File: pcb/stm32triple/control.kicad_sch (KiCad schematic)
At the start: 25 parts, among them J1 USB_C_Receptacle_USB2.0, P1 ST-Link, P2 ST-Link, P3 UG-2864ASWPG01, SW1 RotaryEncoder_Switch, U1 STM32G431CBUx, U3 BME680, U7 TPS82130

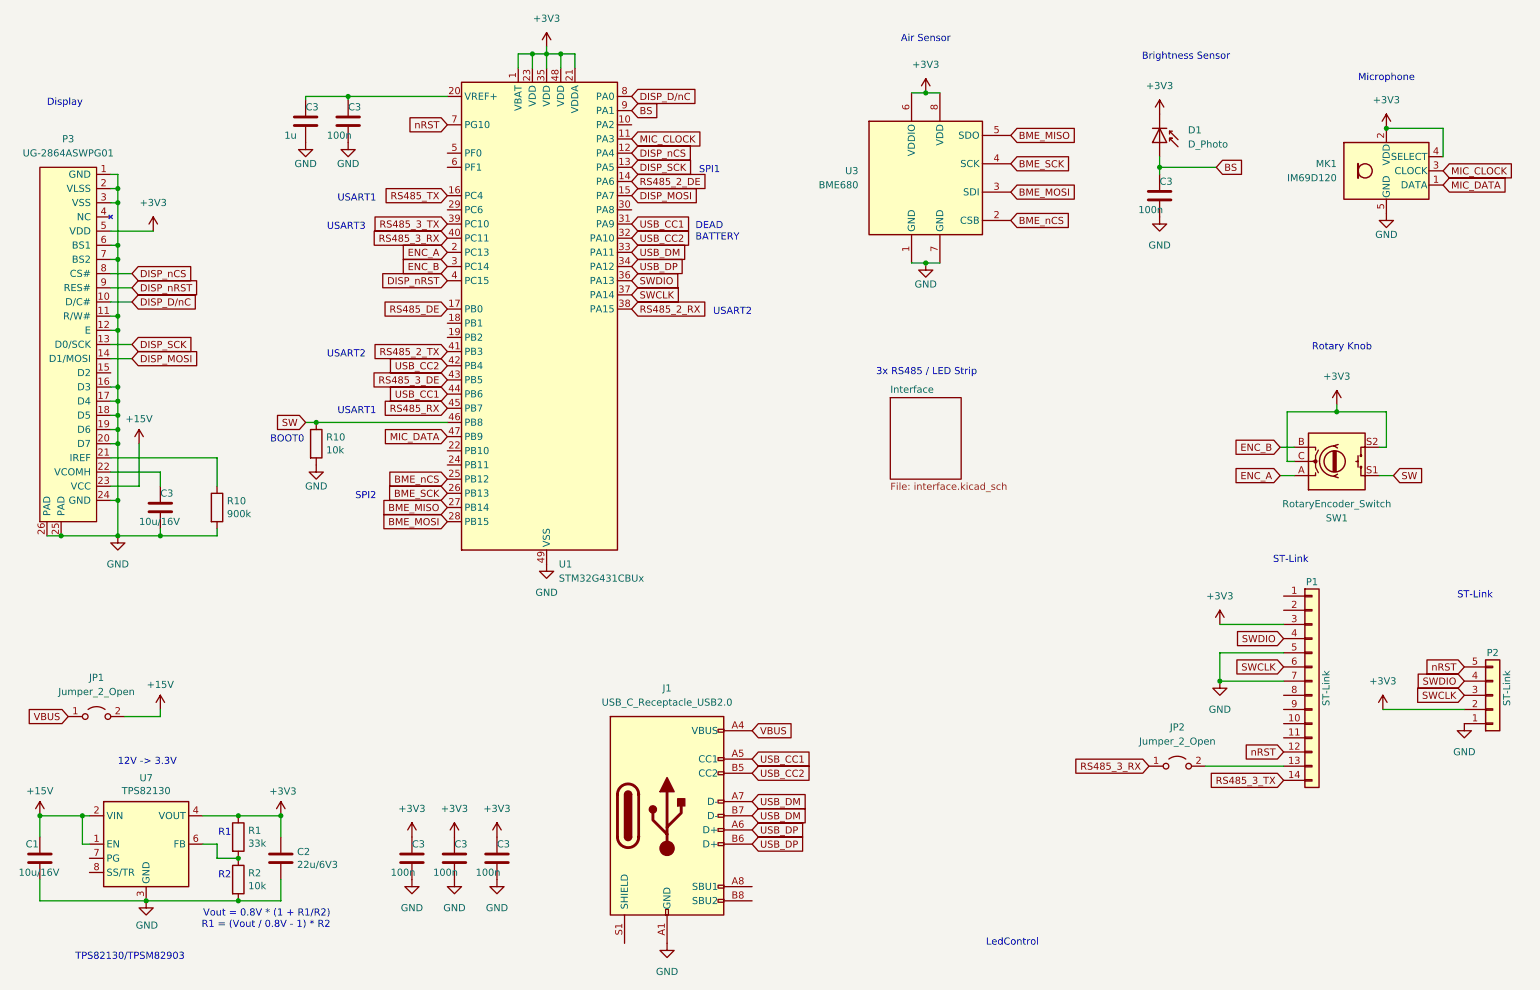
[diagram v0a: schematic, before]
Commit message: Add IR receiver
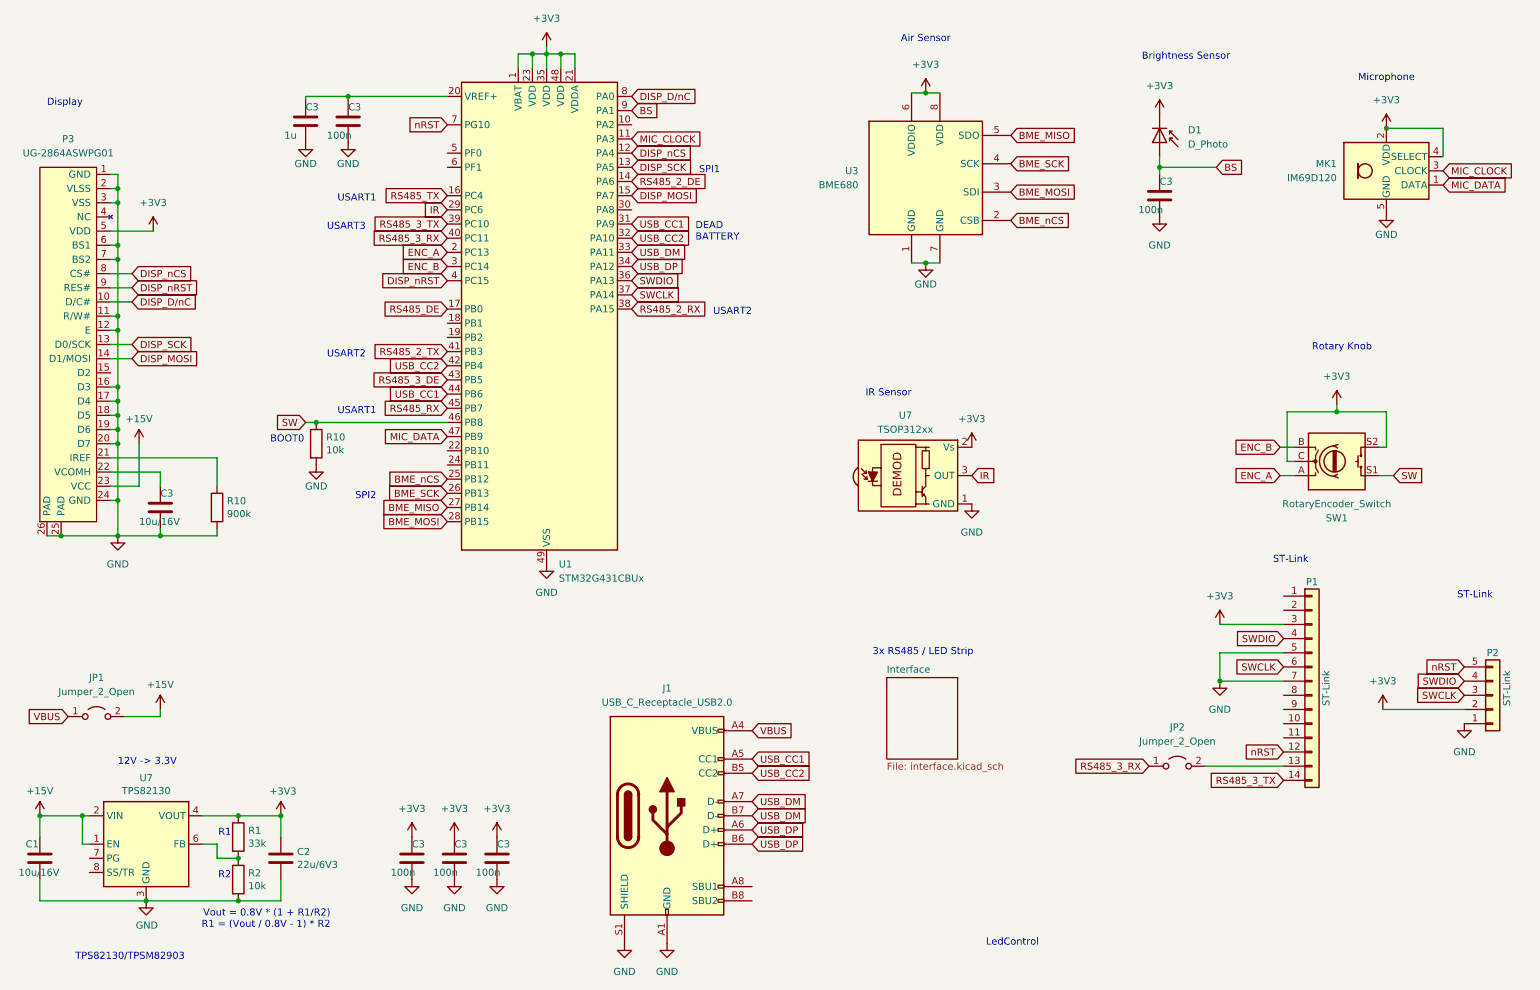
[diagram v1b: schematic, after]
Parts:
- added U7: TSOP312xx, local:TSOP31238, symbol Interface_Optical:TSOP312xx
- J1: footprint local:USB4510-03-1-A -> local:USB4105-GF-A-120
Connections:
- net +3V3: now also U7.2 (Vs)
- net GND: now also J1.S1 (SHIELD), U7.1 (GND)
- net IR: now reaches U1.29 (PC6)
- net IR: now also U7.3 (OUT)
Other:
- note added: "IR Sensor"
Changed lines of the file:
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@@
     (effects (font (size 1.27 1.27)) (justify left bottom))
   )
-  (text "3x RS485 / LED Strip" (at 168.91 88.265 0)
+  (text "3x RS485 / LED Strip" (at 168.275 138.43 0)
     (effects (font (size 1.27 1.27)) (justify left bottom))
   )
@@
     (effects (font (size 1.27 1.27)) (justify left bottom))
   )
+  (text "IR Sensor" (at 167.005 92.075 0)
+    (effects (font (size 1.27 1.27)) (justify left bottom))
+  )
   (text "SPI1" (at 137.16 52.07 0)
     (effects (font (size 1.27 1.27)) (justify left bottom))
@@
     )
   )
+  (global_label "IR" (shape input) (at 186.055 106.045 0) (fields_autoplaced)
+    (effects (font (size 1.27 1.27)) (justify left))
+    (property "Intersheetrefs" "${INTERSHEET_REFS}" (at 190.915 106.045 0)
+      (effects (font (size 1.27 1.27)) (justify left) hide)
+    )
+  )
   (global_label "RS485_3_DE" (shape input) (at 92.075 88.9 180)
     (effects (font (size 1.27 1.27)) (justify right))
@@
     (property "Intersheetrefs" "${INTERSHEET_REFS}" (at 136.6073 63.5 0)
       (effects (font (size 1.27 1.27)) (justify left) hide)
+    )
+  )
+  (global_label "IR" (shape input) (at 92.075 58.42 180) (fields_autoplaced)
+    (effects (font (size 1.27 1.27)) (justify right))
+    (property "Intersheetrefs" "${INTERSHEET_REFS}" (at 87.215 58.42 0)
+      (effects (font (size 1.27 1.27)) (justify right) hide)
     )
   )
@@
         (path "/4b540715-c4ed-4902-8525-92fb403f6b2e"
           (reference "U3") (unit 1)
+        )
+      )
+    )
+  )
+  (symbol (lib_id "power:GND") (at 123.825 189.865 0) (unit 1)
+    (in_bom yes) (on_board yes) (dnp no) (fields_autoplaced)
+    (property "Reference" "#PWR010" (at 123.825 196.215 0)
+      (effects (font (size 1.27 1.27)) hide)
+    )
+    (property "Value" "GND" (at 123.825 194.945 0)
+      (effects (font (size 1.27 1.27)))
+    )
+    (property "Footprint" "" (at 123.825 189.865 0)
+      (effects (font (size 1.27 1.27)) hide)
+    )
+    (property "Datasheet" "" (at 123.825 189.865 0)
+      (effects (font (size 1.27 1.27)) hide)
+    )
+    (pin "1")
+    (instances
+      (project "Display"
+        (path "/1d03a724-b61f-4021-9dcb-6a5edf10ce9e"
+          (reference "#PWR010") (unit 1)
+        )
+      )
+      (project "control"
+        (path "/4b540715-c4ed-4902-8525-92fb403f6b2e"
+          (reference "#PWR054") (unit 1)
         )
       )
@@
         (path "/4b540715-c4ed-4902-8525-92fb403f6b2e"
           (reference "#PWR024") (unit 1)
+        )
+      )
+    )
+  )
+  (symbol (lib_id "power:GND") (at 186.055 111.125 0) (unit 1)
+    (in_bom yes) (on_board yes) (dnp no) (fields_autoplaced)
+    (property "Reference" "#PWR010" (at 186.055 117.475 0)
+      (effects (font (size 1.27 1.27)) hide)
+    )
+    (property "Value" "GND" (at 186.055 116.205 0)
+      (effects (font (size 1.27 1.27)))
+    )
+    (property "Footprint" "" (at 186.055 111.125 0)
+      (effects (font (size 1.27 1.27)) hide)
+    )
+    (property "Datasheet" "" (at 186.055 111.125 0)
+      (effects (font (size 1.27 1.27)) hide)
+    )
+    (pin "1")
+    (instances
+      (project "Display"
+        (path "/1d03a724-b61f-4021-9dcb-6a5edf10ce9e"
+          (reference "#PWR010") (unit 1)
+        )
+      )
+      (project "control"
+        (path "/4b540715-c4ed-4902-8525-92fb403f6b2e"
+          (reference "#PWR052") (unit 1)
         )
       )
@@
     )
   )
+  (symbol (lib_id "power:+3V3") (at 186.055 100.965 0) (unit 1)
+    (in_bom yes) (on_board yes) (dnp no) (fields_autoplaced)
+    (property "Reference" "#PWR02" (at 186.055 104.775 0)
+      (effects (font (size 1.27 1.27)) hide)
+    )
+    (property "Value" "+3V3" (at 186.055 95.885 0)
+      (effects (font (size 1.27 1.27)))
+    )
+    (property "Footprint" "" (at 186.055 100.965 0)
+      (effects (font (size 1.27 1.27)) hide)
+    )
+    (property "Datasheet" "" (at 186.055 100.965 0)
+      (effects (font (size 1.27 1.27)) hide)
+    )
+    (pin "1")
+    (instances
+      (project "Display"
+        (path "/1d03a724-b61f-4021-9dcb-6a5edf10ce9e"
+          (reference "#PWR02") (unit 1)
+        )
+      )
+      (project "control"
+        (path "/4b540715-c4ed-4902-8525-92fb403f6b2e"
+          (reference "#PWR053") (unit 1)
+        )
+      )
+    )
+  )
   (symbol (lib_id "power:+15V") (at 40.64 147.955 0) (unit 1)
     (in_bom yes) (on_board yes) (dnp no) (fields_autoplaced)
@@
         (path "/4b540715-c4ed-4902-8525-92fb403f6b2e"
           (reference "#PWR018") (unit 1)
+        )
+      )
+    )
+  )
+  (symbol (lib_id "Interface_Optical:TSOP312xx") (at 175.895 106.045 0) (unit 1)
+    (in_bom yes) (on_board yes) (dnp no) (fields_autoplaced)
+    (property "Reference" "U7" (at 174.16 95.25 0)
+      (effects (font (size 1.27 1.27)))
+    )
+    (property "Value" "TSOP312xx" (at 174.16 97.79 0)
+      (effects (font (size 1.27 1.27)))
+    )
+    (property "Footprint" "local:TSOP31238" (at 174.625 115.57 0)
+      (effects (font (size 1.27 1.27)) hide)
+    )
+    (property "Datasheet" "http://www.vishay.com/docs/82492/tsop312.pdf" (at 192.405 98.425 0)
+      (effects (font (size 1.27 1.27)) hide)
+    )
+    (pin "1")
+    (pin "2")
+    (pin "3")
+    (instances
+      (project "control"
+        (path "/4b540715-c4ed-4902-8525-92fb403f6b2e"
+          (reference "U7") (unit 1)
         )
       )
@@
       (effects (font (size 1.27 1.27)))
     )
-    (property "Footprint" "local:USB4510-03-1-A" (at 135.255 167.005 0)
+    (property "Footprint" "local:USB4105-GF-A-120" (at 135.255 167.005 0)
       (effects (font (size 1.27 1.27)) hide)
     )
@@
     )
   )
-  (sheet (at 171.45 92.075) (size 12.7 14.605) (fields_autoplaced)
+  (sheet (at 170.815 142.24) (size 12.7 14.605) (fields_autoplaced)
     (stroke (width 0.1524) (type solid))
     (fill (color 0 0 0 0.0000))
-    (property "Sheetname" "Interface" (at 171.45 91.3634 0)
+    (property "Sheetname" "Interface" (at 170.815 141.5284 0)
       (effects (font (size 1.27 1.27)) (justify left bottom))
     )
-    (property "Sheetfile" "interface.kicad_sch" (at 171.45 107.2646 0)
+    (property "Sheetfile" "interface.kicad_sch" (at 170.815 157.4296 0)
       (effects (font (size 1.27 1.27)) (justify left top))
     )

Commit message: Control brightness and duraton with remote control
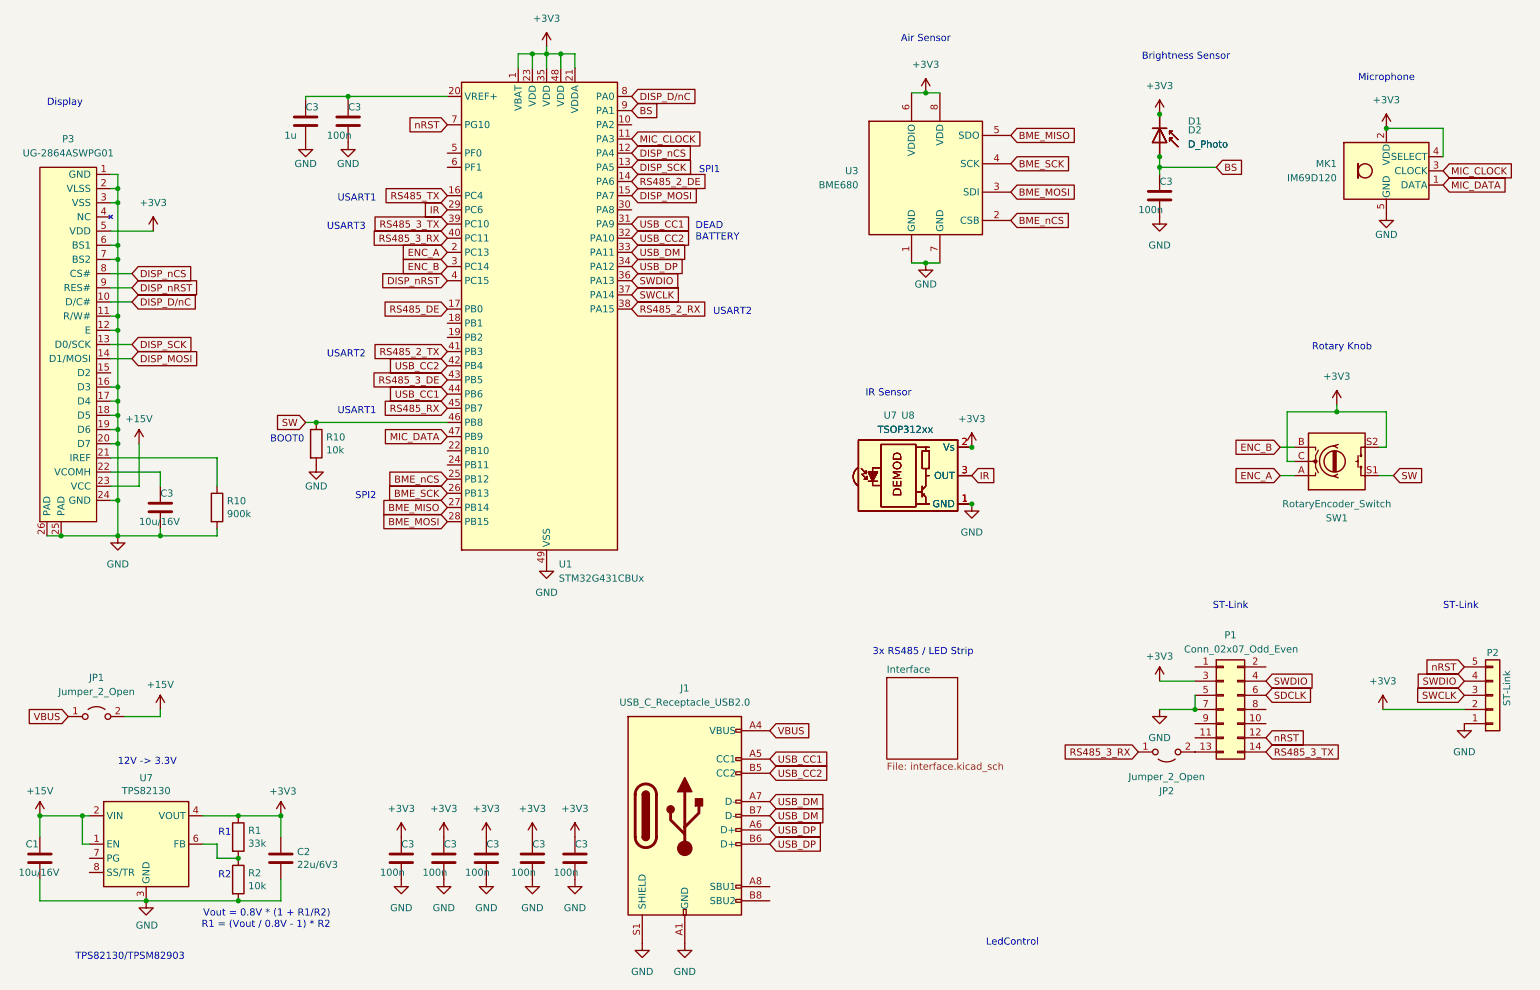
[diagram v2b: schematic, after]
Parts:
- removed P1: ST-Link, local:FTSH-107-01-L-DV-K, symbol Connector_Generic:Conn_01x14
- added C3 (x2): 100n, Capacitor_SMD:C_0603_1608Metric, symbol Device:C
- added D2: D_Photo, local:PhotoDiode, symbol Device:D_Photo
- added P1: Conn_02x07_Odd_Even, local:FTSH-107-01-L-DV-K, symbol Connector_Generic:Conn_02x07_Odd_Even
- added U8: TSOP312xx, local:TSOP31238, symbol Interface_Optical:TSOP312xx
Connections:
- net +3V3: now also C3.1, C3.1, D2.1 (K), P1.3 (Pin_3), U8.2 (Vs)
- net BS: now also D2.2 (A)
- net GND: now also C3.2, C3.2, P1.5 (Pin_5), P1.7 (Pin_7), U8.1 (GND)
- net IR: now also U8.3 (OUT)
- net RS485_3_TX: now also P1.14 (Pin_14)
- net SWDIO: now also P1.4 (Pin_4)
- net nRST: now also P1.12 (Pin_12)
- net at JP2.2 (B): now also P1.13 (Pin_13)
- new net SDCLK: P1.6 (Pin_6)
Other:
- moved on the sheet: C3, J1, JP2

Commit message: Add SnowSparkle, new footprints
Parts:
- C1: footprint Capacitor_SMD:C_1206_3216Metric -> local:1206
- C1: renamed from C3; footprint Capacitor_SMD:C_1206_3216Metric -> local:1206
- C2: renamed from C3; footprint Capacitor_SMD:C_0603_1608Metric -> local:0603
- C2: footprint Capacitor_SMD:C_0805_2012Metric -> local:0805
- D1, D2, J1, JP1, JP2, P2, SW1, U3, U7, U8: now left out of the parts list
- MK1: now not fitted
- P1: value Conn_02x07_Odd_Even -> FTSH-107-01-L-DV-K; footprint local:FTSH-107-01-L-DV-K -> local:PinHeader-2x7-1.27mm-smd
- P3: value UG-2864ASWPG01 -> AFC07-S24FCC-00; footprint local:Connector-Flat-24_P0.5mm -> local:Connector-Flat-24-0.5mm
- R1, R2: footprint Resistor_SMD:R_0603_1608Metric -> local:0603
- R1: renamed from R10; footprint Resistor_SMD:R_0603_1608Metric -> local:0603
- renumbered U7 to U2
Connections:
- net SDCLK is gone; now on net SWCLK: P1.6 (Pin_6)
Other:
- note added: "Display UG-2864ASWPG01"
- note removed: "Display"
